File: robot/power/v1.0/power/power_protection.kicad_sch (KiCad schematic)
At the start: 29 parts, among them Q1 BSC070N10NS5, Q2 BSC070N10NS5, Q3 2N7002, Q4 MMBT5401LT1G, SW1 HDR_2P, SW2 CPG151101D91, U3 LTC2955-2

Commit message: power schematic work
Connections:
- net SENSE: no longer names the net of R2.2, R3.2, U2.1 (SENSE)
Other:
- note added: "18.0 - 30.0V, 30A cont."
- note added: "30A continuous as configured"
- note added: "Power Button Controller and uC Interface"
- moved on the sheet: C1, C2, C3, C4, C5, D1, D2, D3, Q1, Q2, Q3, Q4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

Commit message: power board work
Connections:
- net V_{BATT(PROTECTED)}: no longer R10.1
- net SOME_3v3_TODO renamed +3.3V_LOCAL
- net +3.3V_LOCAL: no longer R13.1
- new net +3.3V_LOCAL_ALWAYS_ON: R10.1, R13.1
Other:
- moved on the sheet: D2
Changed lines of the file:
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@@
 	)
 	(junction
-		(at 165.1 64.77)
+		(at 180.34 64.77)
 		(diameter 0.9144)
 		(color 0 0 0 0)
@@
 	)
 	(junction
-		(at 139.7 64.77)
-		(diameter 0)
-		(color 0 0 0 0)
-	)
-	(junction
 		(at 274.32 49.53)
 		(diameter 0)
@@
 	)
 	(junction
-		(at 186.69 195.58)
-		(diameter 0)
-		(color 0 0 0 0)
-	)
-	(junction
 		(at 77.47 97.79)
 		(diameter 0)
@@
 	(wire
 		(pts
-			(xy 124.46 64.77) (xy 139.7 64.77)
-		)
-		(stroke
-			(width 0)
-			(type default)
-		)
-	)
-	(wire
-		(pts
 			(xy 114.3 113.03) (xy 114.3 118.11)
 		)
@@
 	(wire
 		(pts
-			(xy 165.1 78.74) (xy 165.1 85.09)
+			(xy 139.7 73.66) (xy 147.32 73.66)
+		)
+		(stroke
+			(width 0)
+			(type default)
+		)
+	)
+	(wire
+		(pts
+			(xy 180.34 78.74) (xy 180.34 85.09)
 		)
 		(stroke
@@
 	(wire
 		(pts
+			(xy 124.46 64.77) (xy 180.34 64.77)
+		)
+		(stroke
+			(width 0)
+			(type default)
+		)
+	)
+	(wire
+		(pts
 			(xy 251.46 66.04) (xy 251.46 63.5)
 		)
@@
 	(wire
 		(pts
-			(xy 165.1 62.23) (xy 165.1 64.77)
+			(xy 180.34 62.23) (xy 180.34 64.77)
 		)
 		(stroke
@@
 	(wire
 		(pts
-			(xy 186.69 195.58) (xy 186.69 198.12)
+			(xy 186.69 190.5) (xy 186.69 198.12)
 		)
 		(stroke
@@
 	(wire
 		(pts
-			(xy 165.1 64.77) (xy 165.1 71.12)
+			(xy 180.34 64.77) (xy 180.34 71.12)
 		)
 		(stroke
@@
 	(wire
 		(pts
-			(xy 176.53 195.58) (xy 186.69 195.58)
-		)
-		(stroke
-			(width 0)
-			(type default)
-		)
-	)
-	(wire
-		(pts
 			(xy 120.65 64.77) (xy 124.46 64.77)
 		)
@@
 	(wire
 		(pts
-			(xy 165.1 64.77) (xy 170.18 64.77)
+			(xy 180.34 64.77) (xy 185.42 64.77)
 		)
 		(stroke
@@
 	(wire
 		(pts
-			(xy 186.69 195.58) (xy 193.04 195.58)
+			(xy 186.69 190.5) (xy 194.31 190.5)
 		)
 		(stroke
@@
 	(wire
 		(pts
-			(xy 139.7 64.77) (xy 139.7 81.28)
-		)
-		(stroke
-			(width 0)
-			(type default)
-		)
-	)
-	(wire
-		(pts
 			(xy 58.42 199.39) (xy 58.42 201.93)
 		)
@@
 	(wire
 		(pts
-			(xy 139.7 64.77) (xy 165.1 64.77)
-		)
-		(stroke
-			(width 0)
-			(type default)
-		)
-	)
-	(wire
-		(pts
 			(xy 176.53 205.74) (xy 191.77 205.74)
 		)
@@
 	(wire
 		(pts
+			(xy 139.7 73.66) (xy 139.7 81.28)
+		)
+		(stroke
+			(width 0)
+			(type default)
+		)
+	)
+	(wire
+		(pts
 			(xy 153.67 199.39) (xy 161.29 199.39)
 		)
@@
 	(text_box "~{EN} has a FET controller 900k internet pullup and low-impedance FET to ground. This probably means the stand by current draw gate leakage which is negligible.\n\n~{EN} will rise to V_{batt}"
 		(exclude_from_sim no)
-		(at 147.955 175.26 0)
+		(at 119.38 175.26 0)
 		(size 40.005 16.51)
 		(stroke
@@
 	(text "30A continuous as configured"
 		(exclude_from_sim no)
-		(at 188.976 59.436 0)
+		(at 204.216 59.436 0)
 		(effects
 			(font
@@
 		)
 	)
-	(global_label "SOME_3v3_TODO"
+	(global_label "+3.3V_LOCAL_ALWAYS_ON"
 		(shape input)
-		(at 193.04 195.58 0)
+		(at 147.32 73.66 0)
 		(fields_autoplaced yes)
 		(effects
@@
 		)
 		(property "Intersheetrefs" "${INTERSHEET_REFS}"
-			(at 211.386 195.58 0)
+			(at 174.2539 73.66 0)
+			(effects
+				(font
+					(size 1.27 1.27)
+				)
+				(justify left)
+				(hide yes)
+			)
+		)
+	)
+	(global_label "+3.3V_LOCAL_ALWAYS_ON"
+		(shape input)
+		(at 194.31 190.5 0)
+		(fields_autoplaced yes)
+		(effects
+			(font
+				(size 1.27 1.27)
+			)
+			(justify left)
+		)
+		(property "Intersheetrefs" "${INTERSHEET_REFS}"
+			(at 221.2439 190.5 0)
 			(effects
 				(font
@@
 	(hierarchical_label "V_{BATT(PROTECTED)}"
 		(shape output)
-		(at 170.18 64.77 0)
+		(at 185.42 64.77 0)
 		(fields_autoplaced yes)
 		(effects
@@
 	)
 	(symbol
+		(lib_id "power:+3.3V")
+		(at 176.53 195.58 0)
+		(unit 1)
+		(exclude_from_sim no)
+		(in_bom yes)
+		(on_board yes)
+		(dnp no)
+		(fields_autoplaced yes)
+		(property "Reference" "#PWR056"
+			(at 176.53 199.39 0)
+			(effects
+				(font
+					(size 1.27 1.27)
+				)
+				(hide yes)
+			)
+		)
+		(property "Value" "+3.3V_LOCAL"
+			(at 176.53 190.5 0)
+			(effects
+				(font
+					(size 1.27 1.27)
+				)
+			)
+		)
+		(property "Footprint" ""
+			(at 176.53 195.58 0)
+			(effects
+				(font
+					(size 1.27 1.27)
+				)
+				(hide yes)
+			)
+		)
+		(property "Datasheet" ""
+			(at 176.53 195.58 0)
+			(effects
+				(font
+					(size 1.27 1.27)
+				)
+				(hide yes)
+			)
+		)
+		(property "Description" "Power symbol creates a global label with name \"+3.3V\""
+			(at 176.53 195.58 0)
+			(effects
+				(font
+					(size 1.27 1.27)
+				)
+				(hide yes)
+			)
+		)
+		(pin "1"
+		)
+		(instances
+			(project "power"
+				(path "/4cdb9584-19eb-413c-93c9-302dd5f1c78c/1fec5463-8912-483c-b44e-100b30634a16"
+					(reference "#PWR056")
+					(unit 1)
+				)
+			)
+		)
+	)
+	(symbol
 		(lib_id "power:PWR_FLAG")
 		(at 66.04 196.85 0)
@@
 	(symbol
 		(lib_id "Device:D_TVS")
-		(at 165.1 74.93 90)
+		(at 180.34 74.93 90)
 		(unit 1)
 		(exclude_from_sim no)
@@
 		(dnp no)
 		(property "Reference" "D2"
-			(at 167.64 73.6599 90)
+			(at 182.88 73.6599 90)
 			(effects
 				(font
@@
 		)
 		(property "Value" "SMBJ28CA"
-			(at 167.64 76.2 90)
+			(at 182.88 76.2 90)
 			(effects
 				(font
@@
 		)
 		(property "Footprint" "AT-Discrete:D_SMB_Non-Polar"
-			(at 165.1 74.93 0)
+			(at 180.34 74.93 0)
 			(effects
 				(font
@@
 		)
 		(property "Datasheet" "~"
-			(at 165.1 74.93 0)
+			(at 180.34 74.93 0)
 			(effects
 				(font
@@
 		)
 		(property "Description" ""
-			(at 165.1 74.93 0)
+			(at 180.34 74.93 0)
 			(effects
 				(font
@@
 		)
 		(property "V_{BR}" "V_{BR}=31.1V"
-			(at 172.72 78.74 90)
+			(at 187.96 78.74 90)
 			(effects
 				(font
@@
 		)
 		(property "V_{BR}_min" "V_{BR}_min=28.0"
-			(at 165.1 74.93 90)
+			(at 180.34 74.93 90)
 			(effects
 				(font
@@
 		)
 		(property "V_{BR}_max" "V_{BR}_max=34.4"
-			(at 165.1 74.93 90)
+			(at 180.34 74.93 90)
 			(effects
 				(font
@@
 	(symbol
 		(lib_id "power:GND")
-		(at 165.1 85.09 0)
+		(at 180.34 85.09 0)
 		(unit 1)
 		(exclude_from_sim no)
@@
 		(fields_autoplaced yes)
 		(property "Reference" "#PWR014"
-			(at 165.1 91.44 0)
+			(at 180.34 91.44 0)
 			(effects
 				(font
@@
 		)
 		(property "Value" "GND"
-			(at 165.1 90.17 0)
+			(at 180.34 90.17 0)
 			(effects
 				(font
@@
 		)
 		(property "Footprint" ""
-			(at 165.1 85.09 0)
+			(at 180.34 85.09 0)
 			(effects
 				(font
@@
 		)
 		(property "Datasheet" ""
-			(at 165.1 85.09 0)
+			(at 180.34 85.09 0)
 			(effects
 				(font
@@
 		)
 		(property "Description" ""
-			(at 165.1 85.09 0)
+			(at 180.34 85.09 0)
 			(effects
 				(font
@@
 	(symbol
 		(lib_id "power:PWR_FLAG")
-		(at 165.1 62.23 0)
+		(at 180.34 62.23 0)
 		(unit 1)
 		(exclude_from_sim no)
@@
 		(fields_autoplaced yes)
 		(property "Reference" "#FLG05"
-			(at 165.1 60.325 0)
+			(at 180.34 60.325 0)
 			(effects
 				(font
@@
 		)
 		(property "Value" "PWR_FLAG"
-			(at 165.1 57.15 0)
+			(at 180.34 57.15 0)
 			(effects
 				(font
@@
 		)
 		(property "Footprint" ""
-			(at 165.1 62.23 0)
+			(at 180.34 62.23 0)
 			(effects
 				(font
@@
 		)
 		(property "Datasheet" "~"
-			(at 165.1 62.23 0)
+			(at 180.34 62.23 0)
 			(effects
 				(font
@@
 		)
 		(property "Description" ""
-			(at 165.1 62.23 0)
+			(at 180.34 62.23 0)
 			(effects
 				(font

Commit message: power schematic work
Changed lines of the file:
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@@
 	(text_box "~{EN} has a FET controller 900k internet pullup and low-impedance FET to ground. This probably means the stand by current draw gate leakage which is negligible.\n\n~{EN} will rise to V_{batt}"
 		(exclude_from_sim no)
-		(at 119.38 175.26 0)
+		(at 120.65 172.72 0)
 		(size 40.005 16.51)
 		(stroke

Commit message: power board work
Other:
- moved on the sheet: SW1
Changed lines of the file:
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@@
 	(wire
 		(pts
-			(xy 88.9 205.74) (xy 104.14 205.74)
+			(xy 87.63 205.74) (xy 104.14 205.74)
 		)
 		(stroke
@@
 	(wire
 		(pts
-			(xy 88.9 205.74) (xy 88.9 208.28)
+			(xy 87.63 205.74) (xy 87.63 208.28)
 		)
 		(stroke
@@
 	(wire
 		(pts
-			(xy 88.9 218.44) (xy 88.9 222.25)
+			(xy 87.63 218.44) (xy 87.63 222.25)
 		)
 		(stroke
@@
 	(symbol
 		(lib_id "power:GND")
-		(at 88.9 222.25 0)
+		(at 87.63 222.25 0)
 		(unit 1)
 		(exclude_from_sim no)
@@
 		(fields_autoplaced yes)
 		(property "Reference" "#PWR07"
-			(at 88.9 228.6 0)
+			(at 87.63 228.6 0)
 			(effects
 				(font
@@
 		)
 		(property "Value" "GND"
-			(at 88.9 227.33 0)
+			(at 87.63 227.33 0)
 			(effects
 				(font
@@
 		)
 		(property "Footprint" ""
-			(at 88.9 222.25 0)
+			(at 87.63 222.25 0)
 			(effects
 				(font
@@
 		)
 		(property "Datasheet" ""
-			(at 88.9 222.25 0)
+			(at 87.63 222.25 0)
 			(effects
 				(font
@@
 		)
 		(property "Description" ""
-			(at 88.9 222.25 0)
+			(at 87.63 222.25 0)
 			(effects
 				(font
@@
 	(symbol
 		(lib_id "Switch:SW_Push")
-		(at 88.9 213.36 90)
+		(at 87.63 213.36 90)
 		(unit 1)
 		(exclude_from_sim no)
@@
 		(dnp no)
 		(property "Reference" "SW1"
-			(at 90.17 212.09 90)
+			(at 88.9 212.09 90)
 			(effects
 				(font
@@
 		)
 		(property "Value" "HDR_2P"
-			(at 90.17 214.63 90)
+			(at 88.9 214.63 90)
 			(effects
 				(font
@@
 		)
 		(property "Footprint" "Connector_PinSocket_2.54mm:PinSocket_1x02_P2.54mm_Vertical"
-			(at 83.82 213.36 0)
+			(at 82.55 213.36 0)
 			(effects
 				(font
@@
 		)
 		(property "Datasheet" "~"
-			(at 83.82 213.36 0)
+			(at 82.55 213.36 0)
 			(effects
 				(font
@@
 		)
 		(property "Description" ""
-			(at 88.9 213.36 0)
+			(at 87.63 213.36 0)
 			(effects
 				(font
@@
 		)
 		(property "Value2" "PWRON_{EXT}"
-			(at 90.17 217.17 90)
+			(at 88.9 217.17 90)
 			(effects
 				(font

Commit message: power schematic work
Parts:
- SW1: footprint Connector_PinSocket_2.54mm:PinSocket_1x02_P2.54mm_Vertical -> Connector_JST:JST_SH_SM02B-SRSS-TB_1x02-1MP_P1.00mm_Horizontal
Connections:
- net V_{BATT} renamed V_{batt}
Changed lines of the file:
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@@
 		)
 	)
-	(hierarchical_label "V_{BATT}"
+	(hierarchical_label "V_{batt}"
+		(shape input)
+		(at 52.07 187.96 180)
+		(fields_autoplaced yes)
+		(effects
+			(font
+				(size 1.27 1.27)
+			)
+			(justify right)
+		)
+	)
+	(hierarchical_label "V_{batt}"
 		(shape input)
 		(at 30.48 64.77 180)
@@
 		)
 	)
-	(hierarchical_label "V_{BATT}"
-		(shape input)
-		(at 52.07 187.96 180)
-		(fields_autoplaced yes)
-		(effects
-			(font
-				(size 1.27 1.27)
-			)
-			(justify right)
-		)
-	)
 	(hierarchical_label "V_{BATT(PROTECTED)}"
 		(shape output)
@@
 			)
 		)
-		(property "Footprint" "Connector_PinSocket_2.54mm:PinSocket_1x02_P2.54mm_Vertical"
+		(property "Footprint" "Connector_JST:JST_SH_SM02B-SRSS-TB_1x02-1MP_P1.00mm_Horizontal"
 			(at 82.55 213.36 0)
 			(effects

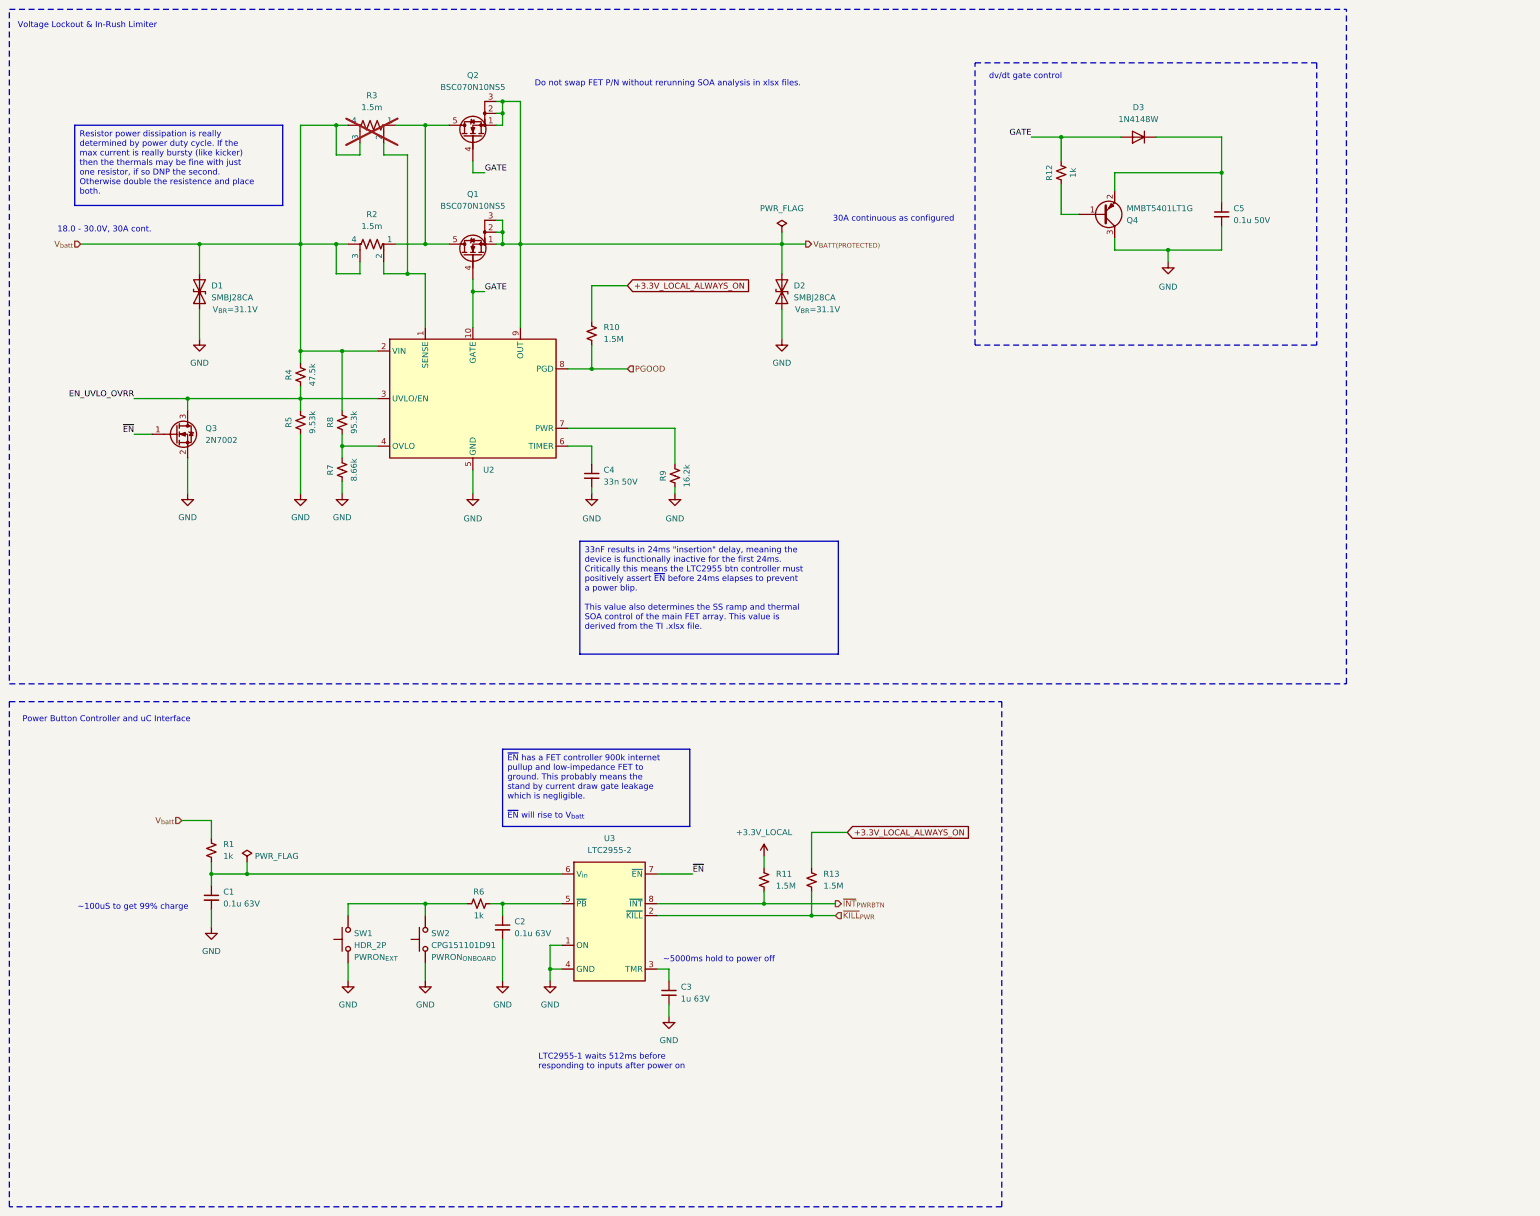
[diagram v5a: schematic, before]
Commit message: passing ERC, footprint work
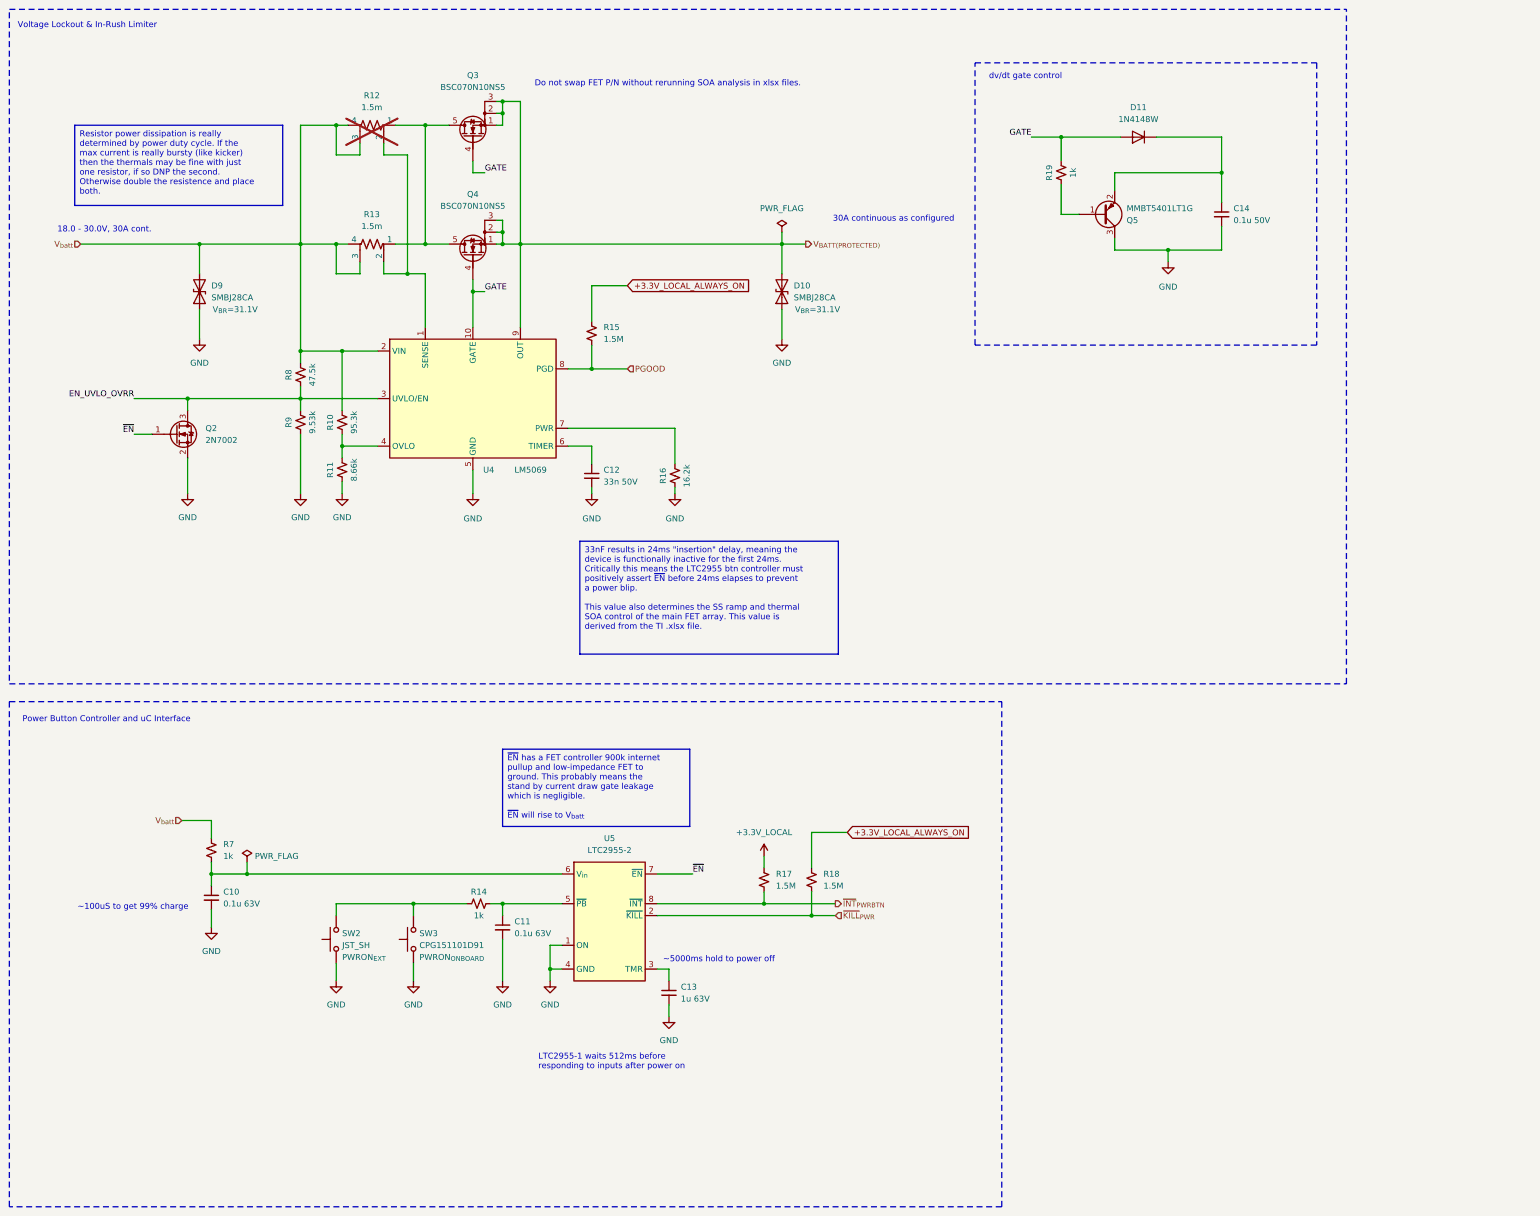
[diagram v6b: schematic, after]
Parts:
- R10: renamed from R8; footprint Resistor_SMD:R_0603_1608Metric -> Resistor_SMD:R_0402_1005Metric
- R11: renamed from R7; footprint Resistor_SMD:R_0603_1608Metric -> Resistor_SMD:R_0402_1005Metric
- R14: renamed from R6; footprint Resistor_SMD:R_0603_1608Metric -> Resistor_SMD:R_0402_1005Metric
- R16: renamed from R9; footprint Resistor_SMD:R_0603_1608Metric -> Resistor_SMD:R_0402_1005Metric
- R19: renamed from R12; footprint Resistor_SMD:R_0603_1608Metric -> Resistor_SMD:R_0402_1005Metric
- R7: renamed from R1; footprint Resistor_SMD:R_0603_1608Metric -> Resistor_SMD:R_0402_1005Metric
- R8: renamed from R4; footprint Resistor_SMD:R_0603_1608Metric -> Resistor_SMD:R_0402_1005Metric
- R9: renamed from R5; footprint Resistor_SMD:R_0603_1608Metric -> Resistor_SMD:R_0402_1005Metric
- SW2: renamed from SW1; value HDR_2P -> JST_SH
- SW3: renamed from SW2; footprint AT-Switches:SW_Kailh_PG1511 -> Button_Switch_SMD:SW_SPST_TL3305A
- U4: renamed from U2; value ~ -> LM5069
- renumbered C1 to C10, C2 to C11, C4 to C12, C3 to C13, C5 to C14, D2 to D10, D3 to D11, D1 to D9, Q3 to Q2, Q2 to Q3, Q1 to Q4, Q4 to Q5, R3 to R12, R2 to R13, R10 to R15, R11 to R17, R13 to R18, U3 to U5
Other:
- company: (none) -> SSL A-Team
- title: (none) -> Power Board
- moved on the sheet: SW2, SW3

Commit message: power board passing ERC/import
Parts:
- removed R12, R13: 1.5m, symbol Device:R_Shunt_US
- added R12, R13: 1.5m, Resistor_SMD:R_2512_6332Metric, symbol Device:R_US
- added TP1: OVLO, TestPoint:TestPoint_Pad_D2.5mm, symbol Connector:TestPoint
- added TP2: EN/UVLO, TestPoint:TestPoint_Pad_D2.5mm, symbol Connector:TestPoint
- added TP3: ~{EN}, TestPoint:TestPoint_Pad_D2.5mm, symbol Connector:TestPoint
- added TP4: GATE/dVdt, TestPoint:TestPoint_Pad_D2.5mm, symbol Connector:TestPoint
- C13: footprint Capacitor_SMD:C_0402_1005Metric -> Capacitor_SMD:C_1206_3216Metric
- Q5: footprint (none) -> Package_TO_SOT_SMD:SOT-23
- U4: footprint (none) -> Package_SO:VSSOP-10_3x3mm_P0.5mm
- U5: footprint (none) -> Package_TO_SOT_SMD:TSOT-23-8_HandSoldering
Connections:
- net EN_UVLO_OVRR: now also TP2.1
- net GATE: now also TP4.1
- net V_{batt}: now also R12.1, R13.1
- net ~{EN}: now also TP3.1
- net at Q3.5 (D), Q4.5 (D): now also U4.1 (SENSE), R12.2, R13.2
- net at R10.2, R11.1, U4.4 (OVLO): now also TP1.1
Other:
- moved on the sheet: C14, D11, Q5, R19
